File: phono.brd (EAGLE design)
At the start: 109.2 x 64.8 mm, 67 parts, among them IC1 NE5532N, IC2 NE5532N, IC3 NE5532N, J1 12VAC, J2 PHONO, J3 OUT, Q1 BC548B, U2 LM317

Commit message: Some tweaks
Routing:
- net N$16: track 52.3 -> 51.6 mm
- net GND: vias 1 -> 92
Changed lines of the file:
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@@
 <via x="60.96" y="53.34" extent="1-16" drill="0.6"/>
 <wire x1="67.31" y1="53.34" x2="60.96" y2="53.34" width="1.778" layer="1"/>
+<via x="-1.27" y="3.81" extent="1-16" drill="0.6"/>
+<via x="-1.27" y="7.62" extent="1-16" drill="0.6"/>
+<via x="-1.27" y="11.43" extent="1-16" drill="0.6"/>
+<via x="-1.27" y="15.24" extent="1-16" drill="0.6"/>
+<via x="-1.27" y="19.05" extent="1-16" drill="0.6"/>
+<via x="-1.27" y="22.86" extent="1-16" drill="0.6"/>
+<via x="-1.27" y="26.67" extent="1-16" drill="0.6"/>
+<via x="-1.27" y="30.48" extent="1-16" drill="0.6"/>
+<via x="-1.27" y="34.29" extent="1-16" drill="0.6"/>
+<via x="-1.27" y="38.1" extent="1-16" drill="0.6"/>
+<via x="-1.27" y="41.91" extent="1-16" drill="0.6"/>
+<via x="-1.27" y="45.72" extent="1-16" drill="0.6"/>
+<via x="-1.27" y="49.53" extent="1-16" drill="0.6"/>
+<via x="-1.27" y="53.34" extent="1-16" drill="0.6"/>
+<via x="3.81" y="58.42" extent="1-16" drill="0.6"/>
+<via x="7.62" y="58.42" extent="1-16" drill="0.6"/>
+<via x="11.43" y="58.42" extent="1-16" drill="0.6"/>
+<via x="15.24" y="58.42" extent="1-16" drill="0.6"/>
+<via x="19.05" y="58.42" extent="1-16" drill="0.6"/>
+<via x="22.86" y="58.42" extent="1-16" drill="0.6"/>
+<via x="60.96" y="50.8" extent="1-16" drill="0.6"/>
+<via x="59.69" y="52.07" extent="1-16" drill="0.6"/>
+<via x="59.69" y="54.61" extent="1-16" drill="0.6"/>
+<via x="27.305" y="59.055" extent="1-16" drill="0.6"/>
+<via x="31.115" y="59.055" extent="1-16" drill="0.6"/>
+<via x="34.925" y="59.055" extent="1-16" drill="0.6"/>
+<via x="38.735" y="59.055" extent="1-16" drill="0.6"/>
+<via x="42.545" y="59.055" extent="1-16" drill="0.6"/>
+<via x="46.355" y="59.055" extent="1-16" drill="0.6"/>
+<via x="50.165" y="59.055" extent="1-16" drill="0.6"/>
+<via x="53.975" y="59.055" extent="1-16" drill="0.6"/>
+<via x="57.785" y="59.055" extent="1-16" drill="0.6"/>
+<via x="61.595" y="59.055" extent="1-16" drill="0.6"/>
+<via x="66.04" y="41.91" extent="1-16" drill="0.6"/>
+<via x="69.85" y="41.91" extent="1-16" drill="0.6"/>
+<via x="73.66" y="41.91" extent="1-16" drill="0.6"/>
+<via x="73.66" y="33.02" extent="1-16" drill="0.6"/>
+<via x="73.66" y="28.575" extent="1-16" drill="0.6"/>
+<via x="73.66" y="24.765" extent="1-16" drill="0.6"/>
+<via x="73.66" y="20.955" extent="1-16" drill="0.6"/>
+<via x="73.66" y="16.51" extent="1-16" drill="0.6"/>
+<via x="72.39" y="13.97" extent="1-16" drill="0.6"/>
+<via x="67.31" y="13.97" extent="1-16" drill="0.6"/>
+<via x="63.5" y="13.97" extent="1-16" drill="0.6"/>
+<via x="60.96" y="13.97" extent="1-16" drill="0.6"/>
+<via x="44.45" y="13.97" extent="1-16" drill="0.6"/>
+<via x="39.37" y="15.24" extent="1-16" drill="0.6"/>
+<via x="39.37" y="19.05" extent="1-16" drill="0.6"/>
+<via x="39.37" y="38.1" extent="1-16" drill="0.6"/>
+<via x="34.29" y="33.02" extent="1-16" drill="0.6"/>
+<via x="34.29" y="16.51" extent="1-16" drill="0.6"/>
+<via x="41.91" y="24.765" extent="1-16" drill="0.6"/>
+<via x="41.91" y="28.575" extent="1-16" drill="0.6"/>
+<via x="41.91" y="32.385" extent="1-16" drill="0.6"/>
+<via x="31.75" y="28.575" extent="1-16" drill="0.6"/>
+<via x="31.75" y="24.765" extent="1-16" drill="0.6"/>
+<via x="30.48" y="13.97" extent="1-16" drill="0.6"/>
+<via x="26.67" y="13.97" extent="1-16" drill="0.6"/>
+<via x="22.86" y="13.97" extent="1-16" drill="0.6"/>
+<via x="13.97" y="20.32" extent="1-16" drill="0.6"/>
+<via x="13.97" y="17.78" extent="1-16" drill="0.6"/>
+<via x="16.51" y="10.16" extent="1-16" drill="0.6"/>
+<via x="20.32" y="8.89" extent="1-16" drill="0.6"/>
+<via x="24.13" y="8.89" extent="1-16" drill="0.6"/>
+<via x="27.94" y="8.89" extent="1-16" drill="0.6"/>
+<via x="31.75" y="8.89" extent="1-16" drill="0.6"/>
+<via x="35.56" y="8.89" extent="1-16" drill="0.6"/>
+<via x="53.34" y="8.89" extent="1-16" drill="0.6"/>
+<via x="57.15" y="8.89" extent="1-16" drill="0.6"/>
+<via x="60.96" y="8.89" extent="1-16" drill="0.6"/>
+<via x="64.77" y="8.89" extent="1-16" drill="0.6"/>
+<via x="72.39" y="8.89" extent="1-16" drill="0.6"/>
+<via x="19.05" y="54.61" extent="1-16" drill="0.6"/>
+<via x="16.51" y="50.8" extent="1-16" drill="0.6"/>
+<via x="16.51" y="45.72" extent="1-16" drill="0.6"/>
+<via x="16.51" y="39.37" extent="1-16" drill="0.6"/>
+<via x="21.59" y="39.37" extent="1-16" drill="0.6"/>
+<via x="21.59" y="45.085" extent="1-16" drill="0.6"/>
+<via x="60.325" y="40.005" extent="1-16" drill="0.6"/>
+<via x="54.61" y="54.61" extent="1-16" drill="0.6"/>
+<via x="54.61" y="52.07" extent="1-16" drill="0.6"/>
+<via x="54.61" y="49.53" extent="1-16" drill="0.6"/>
+<via x="54.61" y="46.99" extent="1-16" drill="0.6"/>
+<via x="54.61" y="44.45" extent="1-16" drill="0.6"/>
+<via x="54.61" y="41.91" extent="1-16" drill="0.6"/>
+<via x="50.8" y="39.37" extent="1-16" drill="0.6"/>
+<via x="41.91" y="39.37" extent="1-16" drill="0.6"/>
+<via x="48.26" y="39.37" extent="1-16" drill="0.6"/>
+<via x="49.53" y="34.29" extent="1-16" drill="0.6"/>
+<via x="44.45" y="34.29" extent="1-16" drill="0.6"/>
+<via x="33.02" y="41.91" extent="1-16" drill="0.6"/>
 </signal>
 <signal name="N$4">
@@
 <wire x1="40.64" y1="49.53" x2="44.45" y2="53.34" width="0.6096" layer="1" curve="90"/>
 <wire x1="72.39" y1="30.48" x2="69.85" y2="33.02" width="0.6096" layer="1" curve="90"/>
-<wire x1="69.85" y1="33.02" x2="62.23" y2="33.02" width="0.6096" layer="1"/>
-<wire x1="62.23" y1="33.02" x2="55.88" y2="39.37" width="0.6096" layer="1" curve="-90"/>
-<wire x1="55.88" y1="39.37" x2="55.88" y2="52.07" width="0.6096" layer="1"/>
-<wire x1="55.88" y1="52.07" x2="52.07" y2="55.88" width="0.6096" layer="1" curve="90"/>
-<wire x1="52.07" y1="55.88" x2="46.99" y2="55.88" width="0.6096" layer="1"/>
+<wire x1="69.85" y1="33.02" x2="60.96" y2="33.02" width="0.6096" layer="1"/>
+<wire x1="49.53" y1="55.88" x2="46.99" y2="55.88" width="0.6096" layer="1"/>
 <wire x1="46.99" y1="55.88" x2="44.45" y2="53.34" width="0.6096" layer="1" curve="90"/>
+<wire x1="60.96" y1="33.02" x2="58.42" y2="35.56" width="0.6096" layer="1" curve="-90"/>
+<wire x1="58.42" y1="35.56" x2="58.42" y2="36.83" width="0.6096" layer="1"/>
+<wire x1="58.42" y1="36.83" x2="55.88" y2="39.37" width="0.6096" layer="1" curve="90"/>
+<wire x1="55.88" y1="39.37" x2="52.705" y2="42.545" width="0.6096" layer="1" curve="-90"/>
+<wire x1="52.705" y1="42.545" x2="52.705" y2="52.705" width="0.6096" layer="1"/>
+<wire x1="52.705" y1="52.705" x2="49.53" y2="55.88" width="0.6096" layer="1" curve="90"/>
 </signal>
 <signal name="FB2_R">

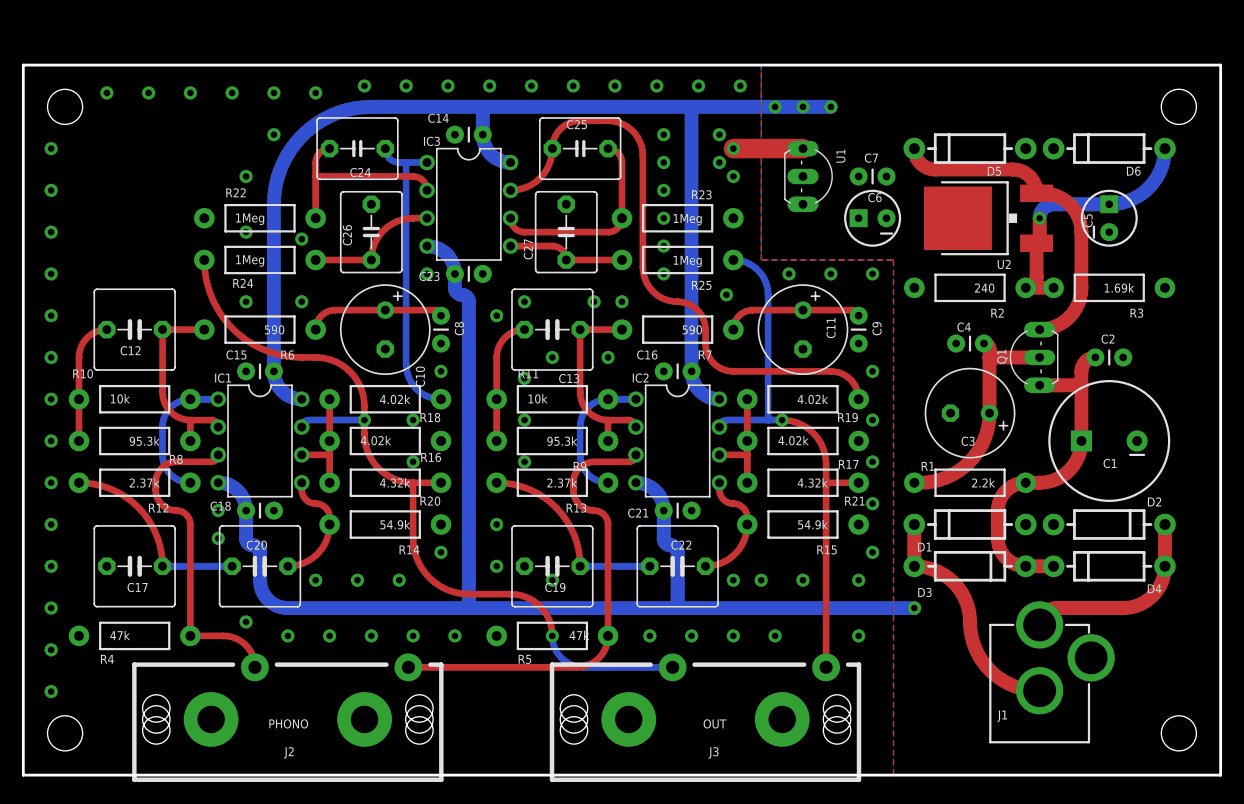
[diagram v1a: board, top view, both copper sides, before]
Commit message: 100p input shunt
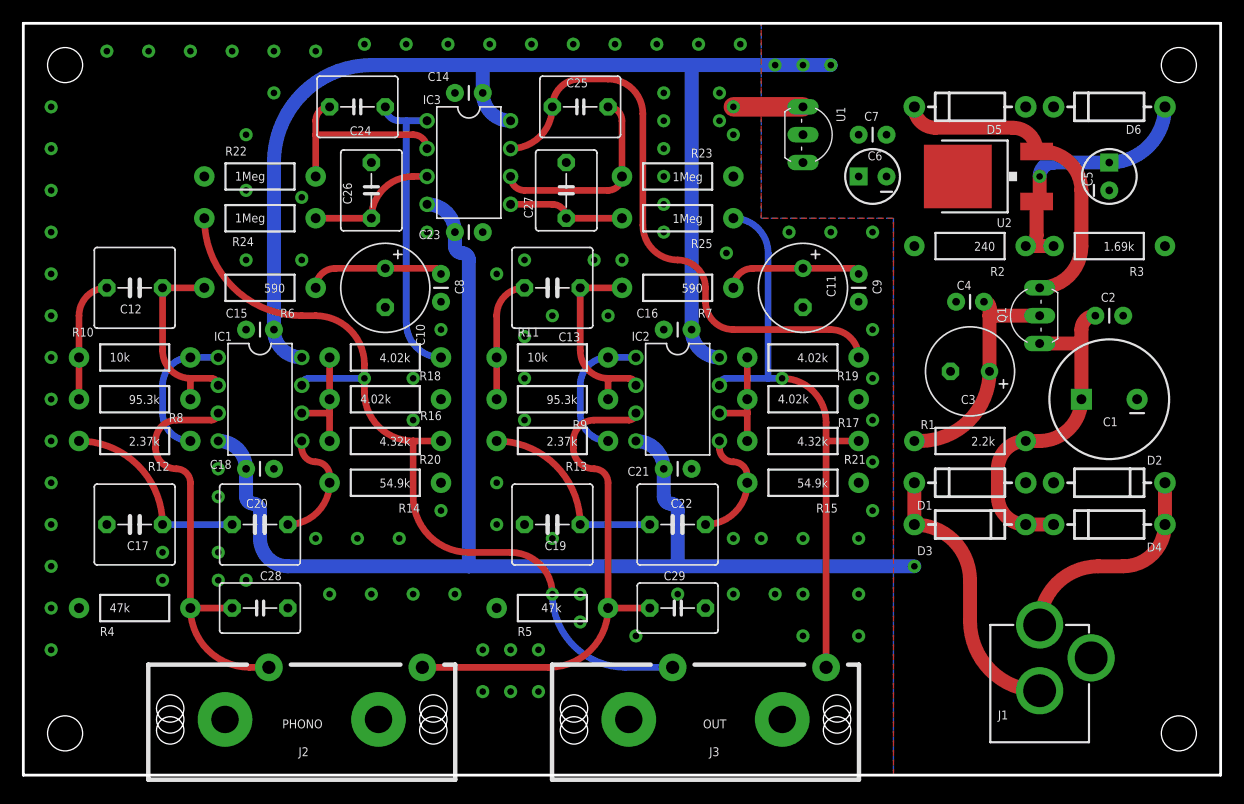
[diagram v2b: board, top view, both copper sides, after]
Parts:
- added C28, C29: 100pF, capacitor-wima:C5B4.5
- moved C10 3.81 mm to (29.2, 40.6)
- moved C11 3.81 mm to (67.3, 40.6)
- moved C12 3.81 mm to (6.35, 40.6)
- moved C13 3.81 mm to (44.5, 40.6)
- moved C14 3.81 mm to (38.1, 58.4)
- moved C2 3.81 mm to (94.0, 38.1)
- moved C23 3.81 mm to (35.6, 45.7)
- moved C26 3.81 mm to (27.9, 49.5)
- moved C27 3.81 mm to (45.7, 49.5)
- moved C3 3.81 mm to (82.5, 33.0)
- moved C7 3.81 mm to (72.4, 54.6)
- moved IC3 3.81 mm to (36.8, 52.1)
- moved Q1 3.81 mm to (87.6, 38.1)
- moved R1 3.81 mm to (82.5, 26.7)
- moved R12 3.81 mm to (6.35, 26.7)
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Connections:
- net GND: now also C28.2, C29.2
- net PH_L: now also C29.1
- net PH_R: now also C28.1
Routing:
- net PH_R: track 29.1 -> 36.5 mm
- net PH_L: track 41.5 -> 46.3 mm
- net OUT_L: track 49.1 -> 52.9 mm
- net HS: track 19.9 -> 23.7 mm
- net OUT_R: track 71.1 -> 72.7 mm
- net LS: track 17.5 -> 19.0 mm
- net GND: vias 92 -> 106
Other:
- board size 109.2 x 64.8 mm -> 109.2 x 68.6 mm
